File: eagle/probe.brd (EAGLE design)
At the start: 21.8 x 21.8 mm, 14 parts

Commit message: probe pcb v1
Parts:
- removed LED10, LED11, LED12, LED13, LED14, LED4, LED5, LED6, LED7, LED8, LED9: (no value), led:LED5MM
- added TO1, TO2, TO3, TO4, TO5, TO6: (no value), general:LED5MM
- UV1, UV2, UV3: device led:LED5MM -> general:LED5MM
- moved UV2 16.5 mm to (18.2, 6.73), turned to 225 degrees
- moved UV1 16.1 mm to (10.9, 19.3)
- moved UV3 14.4 mm to (3.56, 6.86), turned to 135 degrees
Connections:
- new net N$2: TO1.K, TO2.K, TO3.K, TO4.K, TO5.K, TO6.K
- net N$1: now also TO1.A, TO2.A, TO3.A, TO4.A, TO5.A, TO6.A
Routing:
- net N$1: track 0.00 -> 60.2 mm
- net N$2: track 0.00 -> 57.2 mm
- net N$4: track 0.00 -> 57.1 mm, vias 0 -> 1
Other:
- outline, holes or cut-outs redrawn

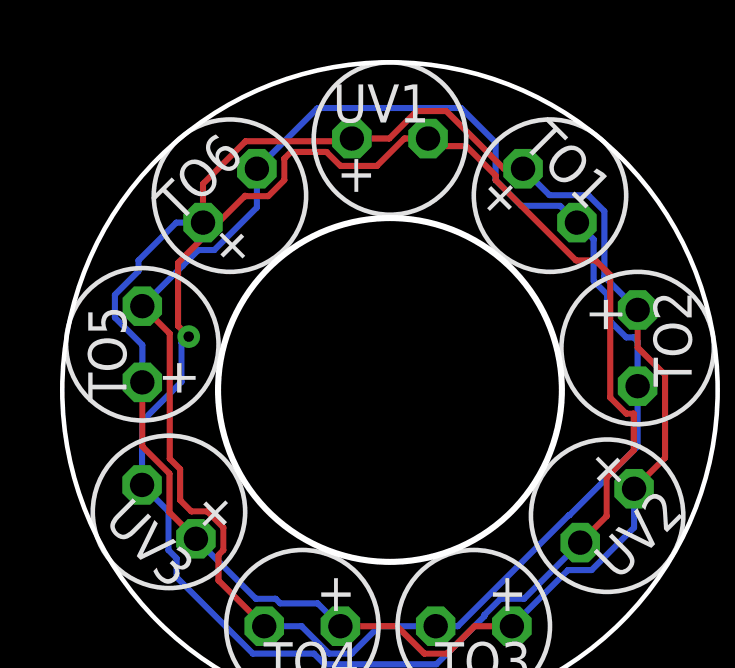
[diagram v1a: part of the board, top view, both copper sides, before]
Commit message: Fix probe pcb bug
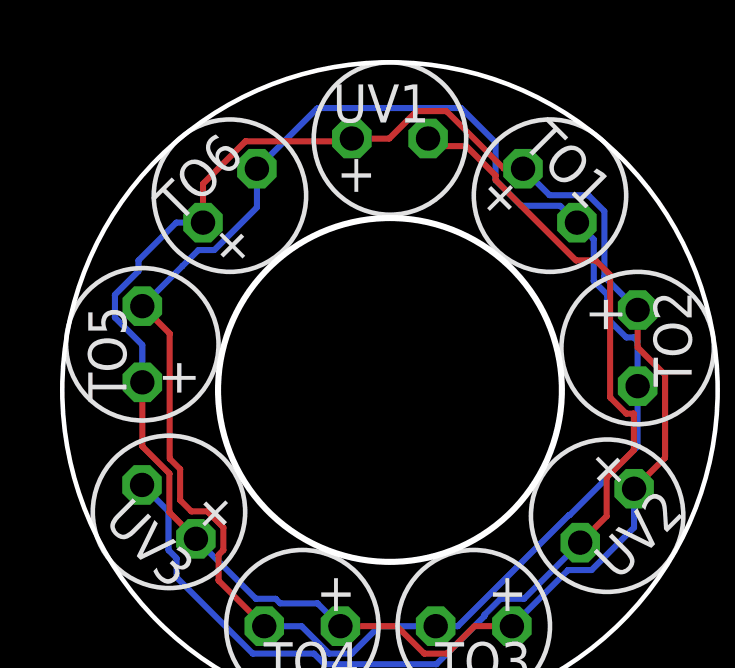
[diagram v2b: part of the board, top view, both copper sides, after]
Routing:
- net N$4: track 57.1 -> 38.1 mm, vias 1 -> 0
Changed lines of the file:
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@@
 <wire x1="6.3522375" y1="2.1336" x2="3.81" y2="4.6758375" width="0.2032" layer="16"/>
 <wire x1="3.81" y1="4.6758375" x2="3.81" y2="5.310834375" width="0.2032" layer="16"/>
-<wire x1="2.657971875" y1="7.756025" x2="2.657971875" y2="9.873809375" width="0.2032" layer="16"/>
-<wire x1="6.093446875" y1="17.396446875" x2="6.107271875" y2="17.382621875" width="0.2032" layer="1"/>
-<wire x1="6.107271875" y1="17.382621875" x2="6.864778125" y2="17.382621875" width="0.2032" layer="1"/>
-<wire x1="6.864778125" y1="17.382621875" x2="7.400428125" y2="17.918271875" width="0.2032" layer="1"/>
-<wire x1="7.400428125" y1="17.918271875" x2="7.400428125" y2="18.636259375" width="0.2032" layer="1"/>
-<wire x1="7.400428125" y1="18.636259375" x2="7.62" y2="18.85583125" width="0.2032" layer="1"/>
-<wire x1="7.62" y1="18.85583125" x2="8.80700625" y2="18.85583125" width="0.2032" layer="1"/>
-<wire x1="8.80700625" y1="18.85583125" x2="9.2732375" y2="18.3896" width="0.2032" layer="1"/>
-<wire x1="11.4017375" y1="19.304" x2="12.192" y2="19.304" width="0.2032" layer="1"/>
-<wire x1="9.2732375" y1="18.3896" x2="10.4873375" y2="18.3896" width="0.2032" layer="1"/>
-<wire x1="10.4873375" y1="18.3896" x2="11.4017375" y2="19.304" width="0.2032" layer="1"/>
-<wire x1="6.093446875" y1="17.396446875" x2="3.858" y2="15.161" width="0.2032" layer="1"/>
-<via x="4.2136" y="12.7" extent="1-16" drill="0.35"/>
-<wire x1="3.9723" y1="11.1881375" x2="3.9723" y2="12.498628125" width="0.2032" layer="16"/>
-<wire x1="3.9723" y1="12.498628125" x2="4.17965625" y2="12.705984375" width="0.2032" layer="16"/>
-<wire x1="2.657971875" y1="9.873809375" x2="3.9723" y2="11.1881375" width="0.2032" layer="16"/>
-<wire x1="3.858" y1="15.161" x2="3.858" y2="13.0556" width="0.2032" layer="1"/>
-<wire x1="3.858" y1="13.0556" x2="4.17965625" y2="12.73394375" width="0.2032" layer="1"/>
-<wire x1="4.17965625" y1="12.73394375" x2="4.17965625" y2="12.705984375" width="0.2032" layer="1"/>
-<wire x1="4.17965625" y1="12.705984375" x2="4.2136" y2="12.7" width="0" layer="19" extent="1-1"/>
 </signal>
 </signals>

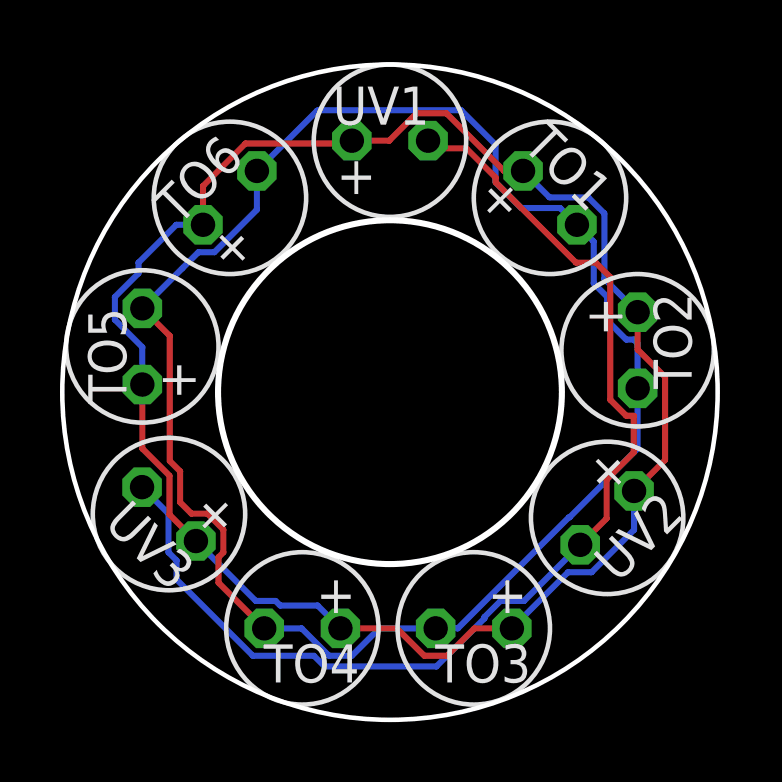
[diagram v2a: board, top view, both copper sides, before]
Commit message: Added laser mount to probe pcb (v2)
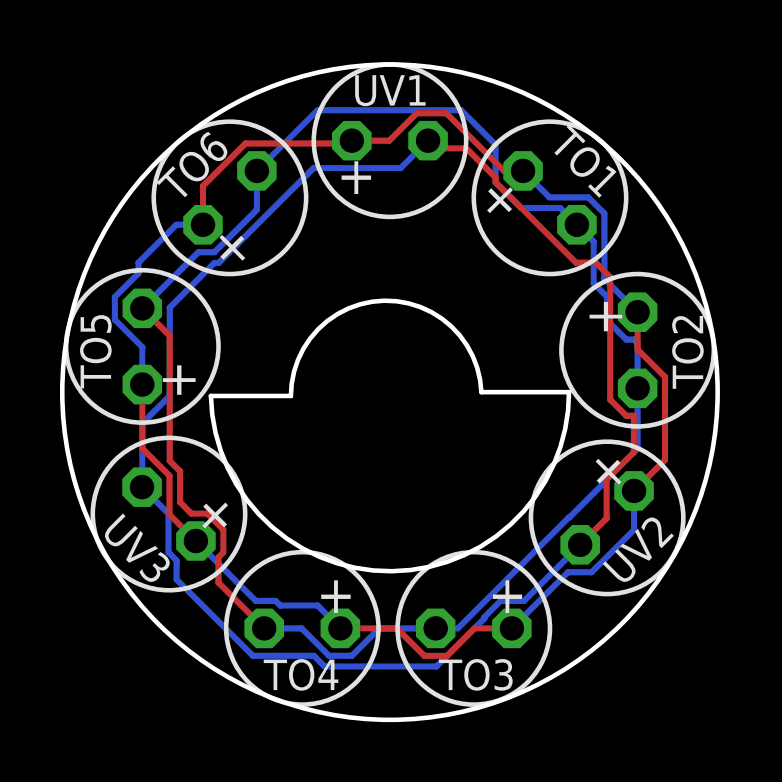
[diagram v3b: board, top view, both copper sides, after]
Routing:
- net N$4: track 38.1 -> 55.4 mm
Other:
- outline, holes or cut-outs redrawn
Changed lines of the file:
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@@
 <setting verticaltext="up"/>
 </settings>
-<grid distance="50" unitdist="mil" unit="mm" style="dots" multiple="1" display="yes" altdistance="5" altunitdist="mil" altunit="mm"/>
+<grid distance="50" unitdist="mil" unit="mm" style="dots" multiple="1" display="yes" altdistance="0.127" altunitdist="mm" altunit="mm"/>
 <layers>
 <layer number="1" name="Top" color="4" fill="1" visible="yes" active="yes"/>
@@
 <plain>
 <circle x="10.922" y="10.922" radius="10.9227375" width="0.1524" layer="20"/>
-<circle x="10.922" y="10.922" radius="5.7305" width="0.2032" layer="20"/>
+<wire x1="7.62" y1="10.795" x2="13.97" y2="10.922" width="0.1524" layer="20" curve="-177.70939"/>
+<wire x1="4.953" y1="10.795" x2="16.891" y2="10.922" width="0.1524" layer="20" curve="178.781125"/>
+<wire x1="4.953" y1="10.795" x2="7.62" y2="10.795" width="0.1524" layer="20"/>
+<wire x1="13.97" y1="10.922" x2="16.891" y2="10.922" width="0.1524" layer="20"/>
 </plain>
 <attributes>
@@
 </class>
 </classes>
-<designrules name="default">
+<designrules name="default *">
 <description language="de">&lt;b&gt;EAGLE Design Rules&lt;/b&gt;
 &lt;p&gt;
@@
 <param name="mdViaViaSameLayer" value="6mil"/>
 <param name="mnLayersViaInSmd" value="2"/>
-<param name="mdCopperDimension" value="40mil"/>
+<param name="mdCopperDimension" value="30mil"/>
 <param name="mdDrill" value="6mil"/>
 <param name="mdSmdStop" value="0mil"/>
@@
 <elements>
 <element name="TO1" library="general" package="LED5MM" package3d_urn="urn:adsk.eagle:package:15799/2" value="" x="16.256" y="17.399" smashed="yes" rot="R315">
-<attribute name="NAME" x="15.2861375" y="19.12320625" size="1.27" layer="25" ratio="10" rot="R315"/>
+<attribute name="NAME" x="16.1751375" y="19.12320625" size="1.016" layer="25" ratio="10" rot="R315"/>
 <attribute name="POPULARITY" value="93" x="16.256" y="17.399" size="1.778" layer="27" rot="R315" display="off"/>
 </element>
 <element name="TO2" library="general" package="LED5MM" package3d_urn="urn:adsk.eagle:package:15799/2" value="" x="19.177" y="12.319" smashed="yes" rot="R270">
-<attribute name="NAME" x="19.710403125" y="14.22399375" size="1.27" layer="25" ratio="10" rot="R270"/>
+<attribute name="NAME" x="20.345403125" y="13.58899375" size="1.016" layer="25" ratio="10" rot="R270"/>
 <attribute name="POPULARITY" value="93" x="19.177" y="12.319" size="1.778" layer="27" rot="R270" display="off"/>
 </element>
 <element name="TO3" library="general" package="LED5MM" package3d_urn="urn:adsk.eagle:package:15799/2" value="" x="13.716" y="3.048" smashed="yes" rot="R180">
-<attribute name="NAME" x="15.621" y="2.514596875" size="1.27" layer="25" ratio="10" rot="R180"/>
+<attribute name="NAME" x="15.113" y="2.006596875" size="1.016" layer="25" ratio="10" rot="R180"/>
 <attribute name="POPULARITY" value="93" x="13.716" y="3.048" size="1.778" layer="27" rot="R180" display="off"/>
 </element>
 <element name="TO4" library="general" package="LED5MM" package3d_urn="urn:adsk.eagle:package:15799/2" value="" x="8.001" y="3.048" smashed="yes" rot="R180">
-<attribute name="NAME" x="9.906" y="2.514596875" size="1.27" layer="25" ratio="10" rot="R180"/>
+<attribute name="NAME" x="9.271" y="2.006596875" size="1.016" layer="25" ratio="10" rot="R180"/>
 <attribute name="POPULARITY" value="93" x="8.001" y="3.048" size="1.778" layer="27" rot="R180" display="off"/>
 </element>
 <element name="TO5" library="general" package="LED5MM" package3d_urn="urn:adsk.eagle:package:15799/2" value="" x="2.667" y="12.446" smashed="yes" rot="R90">
-<attribute name="NAME" x="2.1336" y="10.540996875" size="1.27" layer="25" ratio="10" rot="R90"/>
+<attribute name="NAME" x="1.6256" y="11.048996875" size="1.016" layer="25" ratio="10" rot="R90"/>
 <attribute name="POPULARITY" value="93" x="2.667" y="12.446" size="1.778" layer="27" rot="R90" display="off"/>
 </element>
 <element name="TO6" library="general" package="LED5MM" package3d_urn="urn:adsk.eagle:package:15799/2" value="" x="5.588" y="17.399" smashed="yes" rot="R45">
-<attribute name="NAME" x="3.863790625" y="16.42913125" size="1.27" layer="25" ratio="10" rot="R45"/>
+<attribute name="NAME" x="3.863790625" y="17.19113125" size="1.016" layer="25" ratio="10" rot="R45"/>
 <attribute name="POPULARITY" value="93" x="5.588" y="17.399" size="1.778" layer="27" rot="R45" display="off"/>
 </element>
 <element name="UV1" library="general" package="LED5MM" package3d_urn="urn:adsk.eagle:package:15799/2" value="" x="10.922" y="19.304" smashed="yes">
-<attribute name="NAME" x="9.017" y="19.8374" size="1.27" layer="25" ratio="10"/>
+<attribute name="NAME" x="9.652" y="20.4724" size="1.016" layer="25" ratio="10"/>
 <attribute name="POPULARITY" value="93" x="10.922" y="19.304" size="1.778" layer="27" display="off"/>
 </element>
 <element name="UV2" library="general" package="LED5MM" package3d_urn="urn:adsk.eagle:package:15799/2" value="" x="18.161" y="6.731" smashed="yes" rot="R225">
-<attribute name="NAME" x="19.885209375" y="7.7008625" size="1.27" layer="25" ratio="10" rot="R225"/>
+<attribute name="NAME" x="19.758209375" y="6.9388625" size="1.016" layer="25" ratio="10" rot="R225"/>
 <attribute name="POPULARITY" value="93" x="18.161" y="6.731" size="1.778" layer="27" rot="R225" display="off"/>
 </element>
 <element name="UV3" library="general" package="LED5MM" package3d_urn="urn:adsk.eagle:package:15799/2" value="" x="3.556" y="6.858" smashed="yes" rot="R135">
-<attribute name="NAME" x="4.52586875" y="5.1337875" size="1.27" layer="25" ratio="10" rot="R135"/>
+<attribute name="NAME" x="3.76386875" y="5.1337875" size="1.016" layer="25" ratio="10" rot="R135"/>
 <attribute name="POPULARITY" value="93" x="3.556" y="6.858" size="1.778" layer="27" rot="R135" display="off"/>
 </element>
@@
 <wire x1="12.4691625" y1="1.778" x2="8.7449375" y2="1.778" width="0.2032" layer="16"/>
 <wire x1="3.81" y1="5.310834375" x2="3.53961875" y2="5.581215625" width="0.2032" layer="16"/>
-<wire x1="3.53961875" y1="6.874378125" x2="2.657971875" y2="7.756025" width="0.2032" layer="16"/>
+<wire x1="3.53961875" y1="6.874378125" x2="2.666996875" y2="7.747" width="0.2032" layer="16"/>
+<wire x1="2.666996875" y1="7.747" x2="2.657971875" y2="7.756025" width="0.2032" layer="16"/>
 <wire x1="3.53961875" y1="5.581215625" x2="3.53961875" y2="6.874378125" width="0.2032" layer="16"/>
 <wire x1="6.3522375" y1="2.1336" x2="3.81" y2="4.6758375" width="0.2032" layer="16"/>
 <wire x1="3.81" y1="4.6758375" x2="3.81" y2="5.310834375" width="0.2032" layer="16"/>
+<wire x1="12.192" y1="19.304" x2="11.2776" y2="18.3896" width="0.2032" layer="16"/>
+<wire x1="5.216025" y1="15.230975" x2="5.070975" y2="15.230975" width="0.2032" layer="16"/>
+<wire x1="2.666996875" y1="9.882834375" x2="2.666996875" y2="7.747" width="0.2032" layer="16"/>
+<wire x1="3.5814" y1="10.7972375" x2="2.666996875" y2="9.882834375" width="0.2032" layer="16"/>
+<wire x1="3.5814" y1="13.7414" x2="3.5814" y2="10.7972375" width="0.2032" layer="16"/>
+<wire x1="5.070975" y1="15.230975" x2="3.5814" y2="13.7414" width="0.2032" layer="16"/>
+<wire x1="11.2776" y1="18.3896" x2="8.37465" y2="18.3896" width="0.2032" layer="16"/>
+<wire x1="8.37465" y1="18.3896" x2="5.216025" y2="15.230975" width="0.2032" layer="16"/>
 </signal>
 </signals>

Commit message: Updated probe and rear eagle files
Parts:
- added FACE, REAR: TPTP10R, testpad:TP10R
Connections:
- new net FACE: FACE.TP
- new net REAR: REAR.TP
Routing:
- net N$4: track 55.4 -> 32.2 mm
- net N$1: track 60.2 -> 56.3 mm
- net FACE: track 0.00 -> 3.05 mm, vias 0 -> 2
- net N$2: track 57.2 -> 55.5 mm
- added copper zone on layer 16, net FACE
- added copper zone on layer 1, net REAR

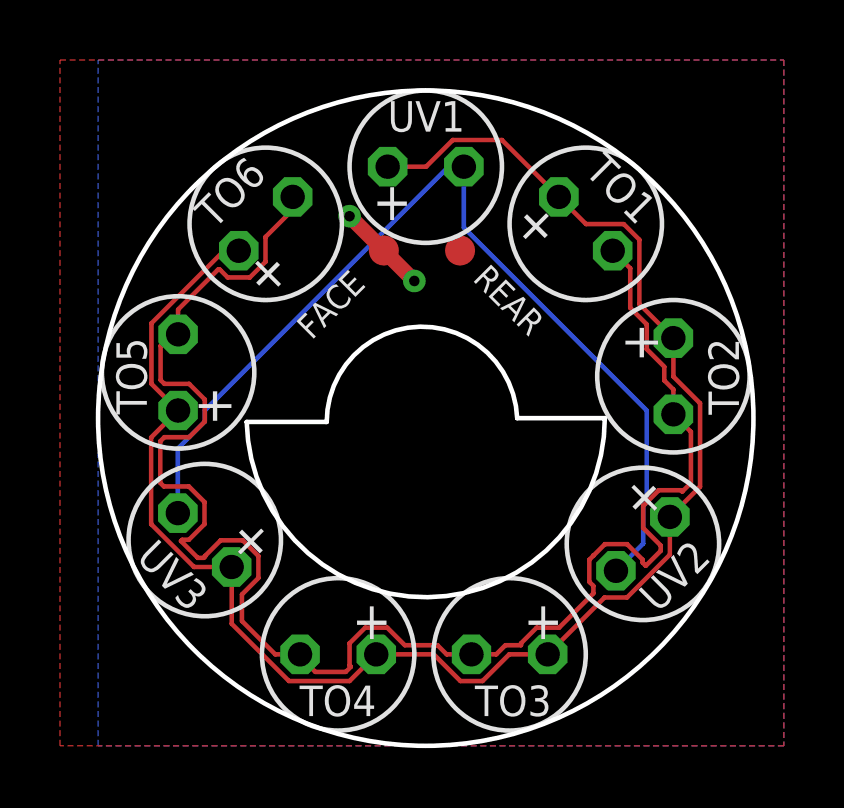
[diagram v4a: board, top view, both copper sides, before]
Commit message: Tweaked probe LED traces
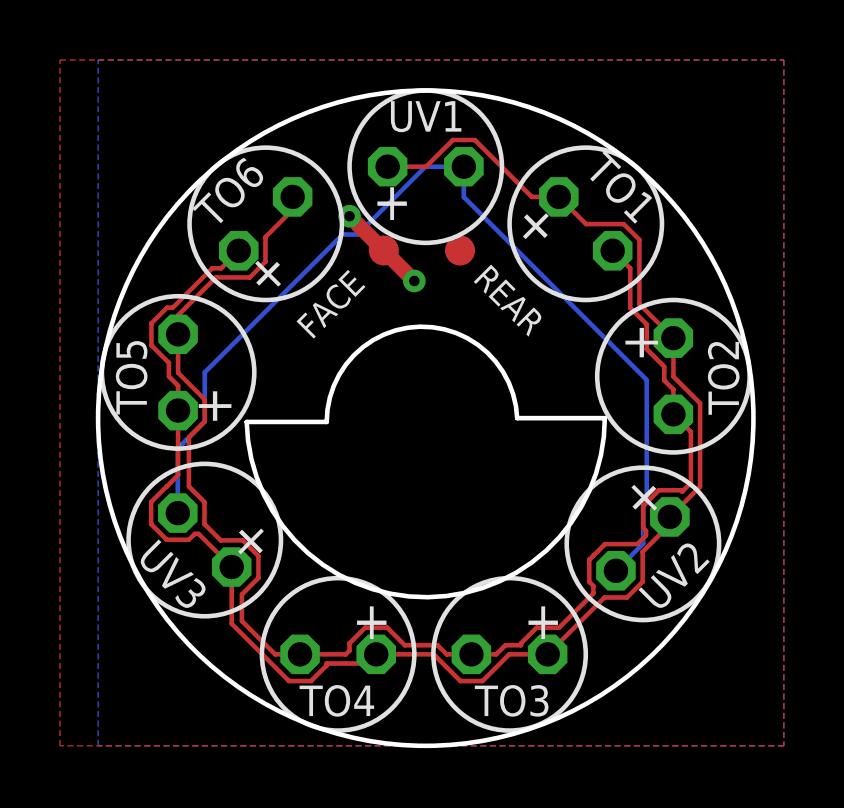
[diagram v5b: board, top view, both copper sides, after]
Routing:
- net N$2: track 55.5 -> 47.7 mm
- net N$4: track 32.2 -> 33.0 mm

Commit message: new pcbs
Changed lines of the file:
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@@
 <param name="mdViaViaSameLayer" value="6mil"/>
 <param name="mnLayersViaInSmd" value="2"/>
-<param name="mdCopperDimension" value="18mil"/>
+<param name="mdCopperDimension" value="20mil"/>
 <param name="mdDrill" value="6mil"/>
 <param name="mdSmdStop" value="0mil"/>
@@
 <wire x1="18.170025" y1="7.997259375" x2="18.170025" y2="6.740025" width="0.1524" layer="16"/>
 <wire x1="2.657971875" y1="7.756025" x2="2.657971875" y2="9.909734375" width="0.1524" layer="16"/>
-<wire x1="2.657971875" y1="9.909734375" x2="3.556" y2="10.8077625" width="0.1524" layer="16"/>
-<wire x1="3.556" y1="10.8077625" x2="3.556" y2="12.446" width="0.1524" layer="16"/>
+<wire x1="3.556" y1="10.8077625" x2="2.657971875" y2="9.909734375" width="0.1524" layer="16"/>
 <wire x1="12.192" y1="18.288" x2="12.192" y2="19.304" width="0.1524" layer="16"/>
 <wire x1="18.288" y1="8.115234375" x2="18.288" y2="12.192" width="0.1524" layer="16"/>
 <wire x1="18.288" y1="12.192" x2="12.192" y2="18.288" width="0.1524" layer="16"/>
-<wire x1="10.9092375" y1="19.304" x2="12.192" y2="19.304" width="0.1524" layer="16"/>
-<wire x1="8.1562" y1="17.0462" x2="8.6514375" y2="17.0462" width="0.1524" layer="16"/>
-<wire x1="8.6514375" y1="17.0462" x2="10.9092375" y2="19.304" width="0.1524" layer="16"/>
-<wire x1="3.556" y1="12.446" x2="8.1562" y2="17.0462" width="0.1524" layer="16"/>
+<wire x1="12.192" y1="19.304" x2="10.9092375" y2="19.304" width="0.1524" layer="16"/>
+<wire x1="3.556" y1="11.9507625" x2="3.556" y2="10.8077625" width="0.1524" layer="16"/>
+<wire x1="10.9092375" y1="19.304" x2="3.556" y2="11.9507625" width="0.1524" layer="16"/>
 </signal>
 <signal name="FACE" class="1">
